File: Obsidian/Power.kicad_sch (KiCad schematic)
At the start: 79 parts, among them J10 Barrel_Jack_Switch, Q4 DMP3013SFV, U10 TPSM863257RDXR, U11 TPSM863257RDXR, U18 TLV77325PDBVR, U20 RT9045AGSP / AP2303, U23 NCV59801CML120TCG, U24 SN74LVC1G07DBV, U25 SN74LVC1G07DBV, U4 TPSM863257RDXR, U5 TPSM863257RDXR, U6 TPSM863257RDXR

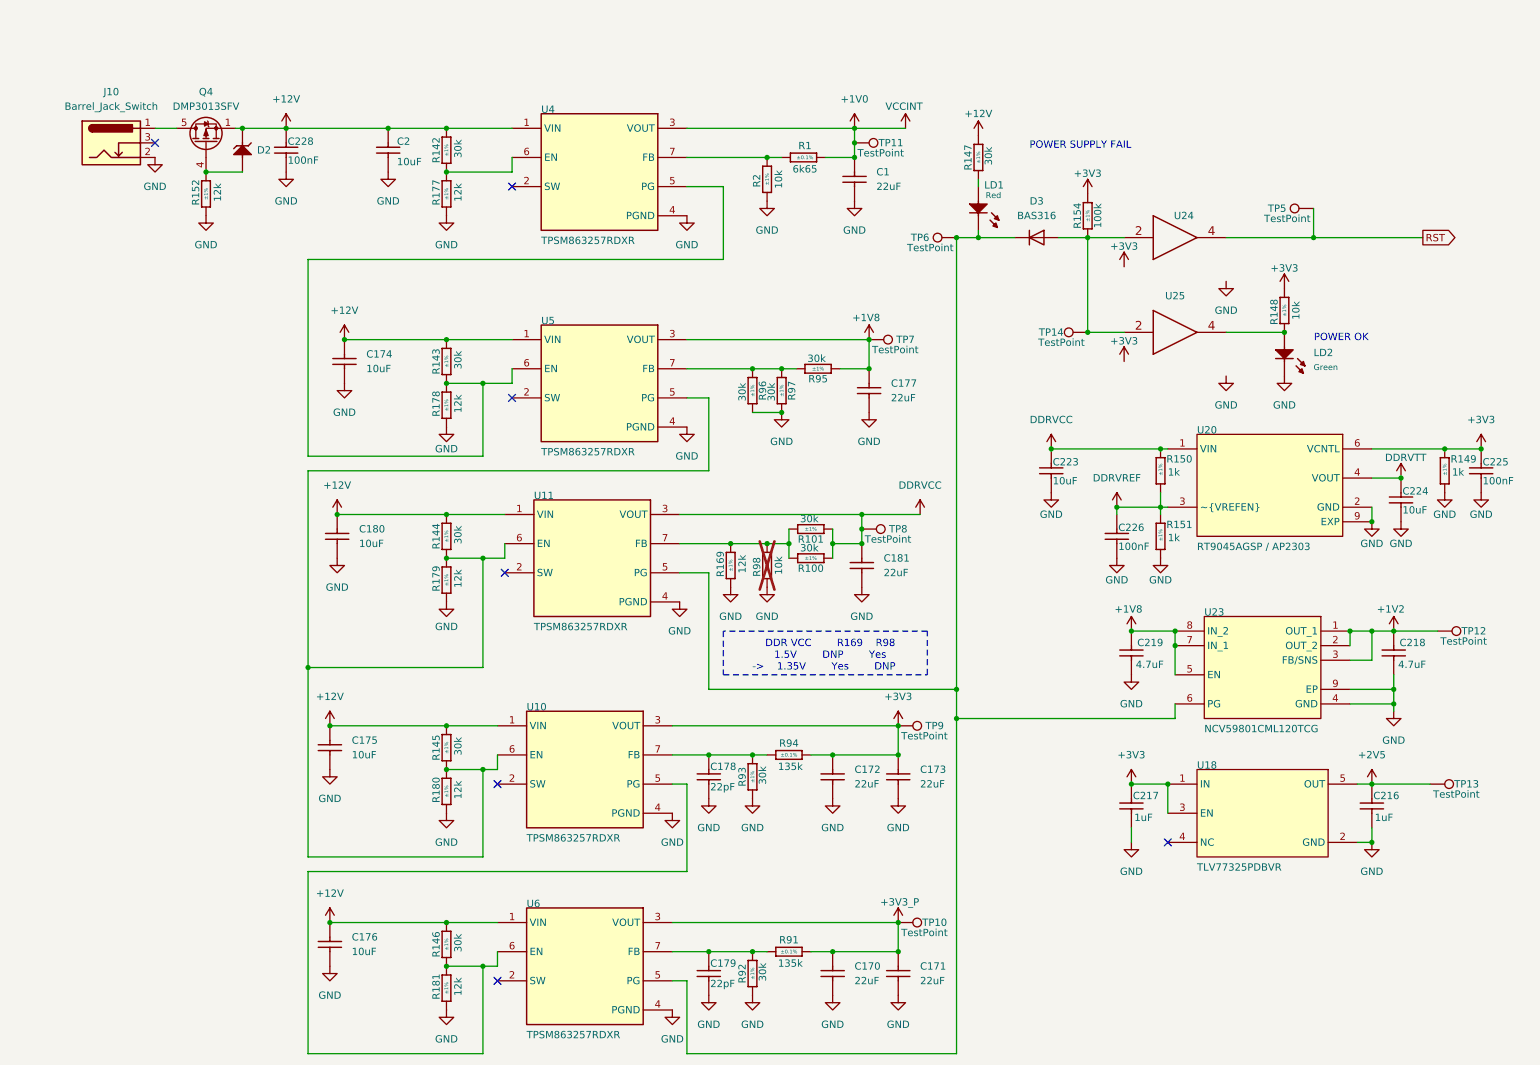
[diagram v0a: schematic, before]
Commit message: update with available components on LCSC
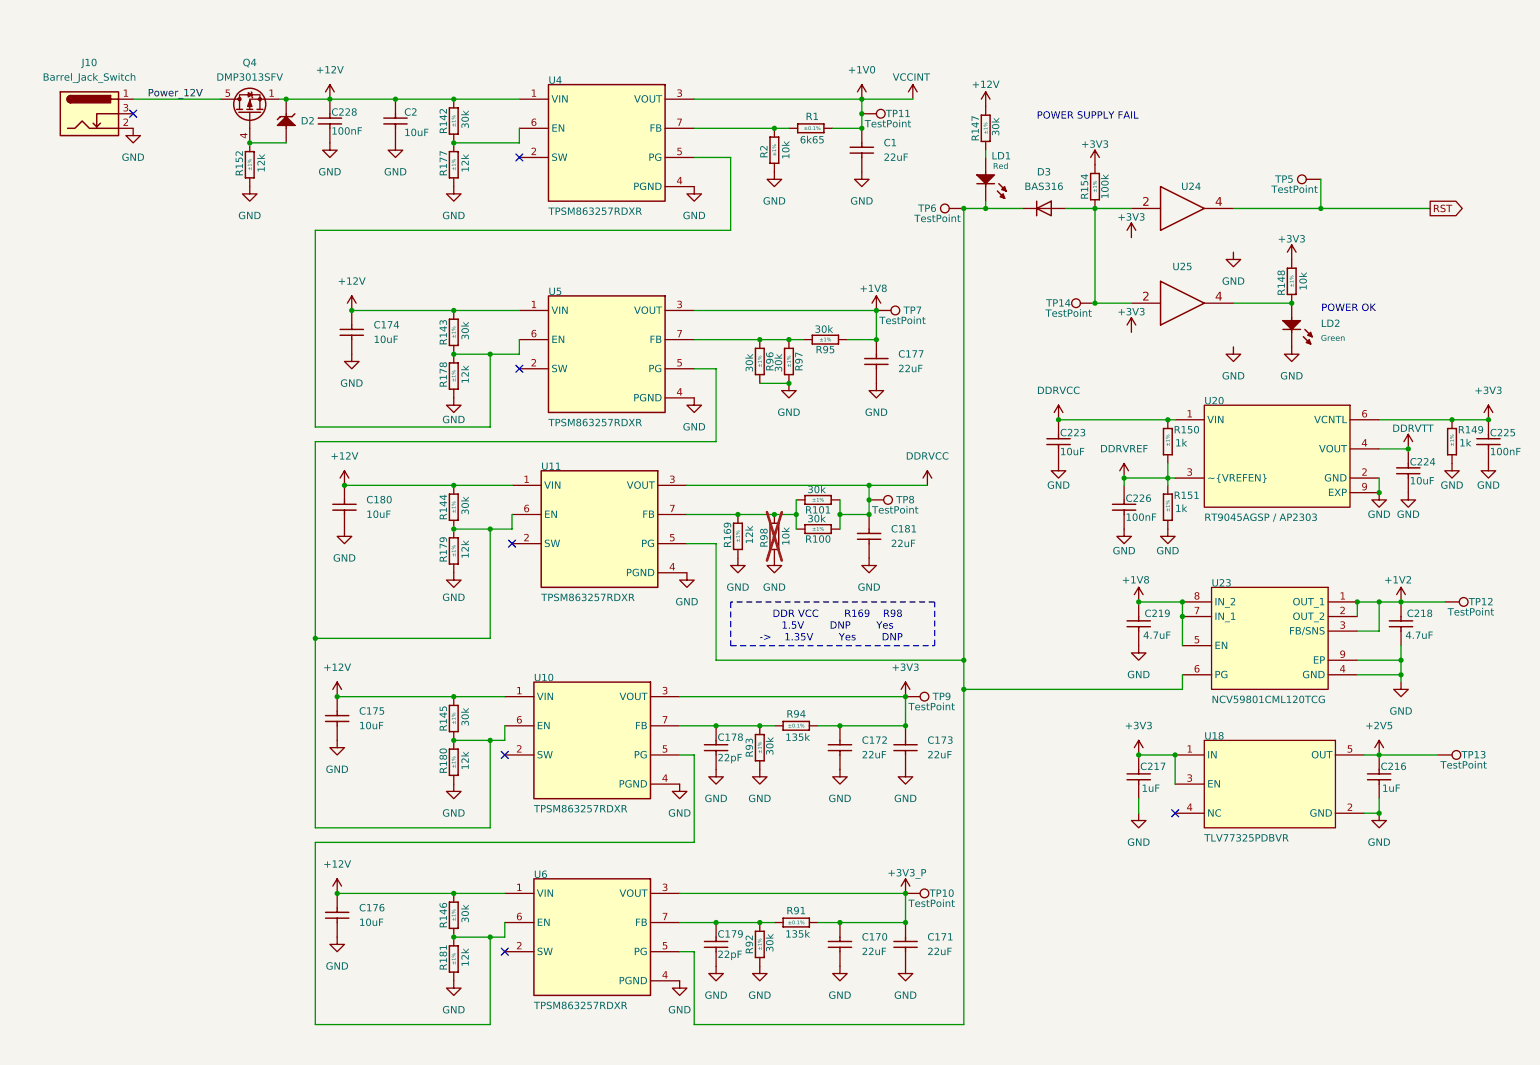
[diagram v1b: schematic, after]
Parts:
- C1, C170, C171, C172, C173, C177, C181: LCSC (none) -> C296720
- C174, C175, C176, C180, C2: LCSC (none) -> C15850
- C178, C179: LCSC (none) -> C1555
- C216, C217: LCSC (none) -> C29266
- C218, C219: LCSC (none) -> C318563
- C223, C224: LCSC (none) -> C76991
- C225, C226, C228: LCSC (none) -> C110251
- D2: FT Rotation Offset (none) -> 0; LCSC (none) -> C891576
- D3: FT Rotation Offset (none) -> 0; LCSC (none) -> C7502720
- J10: LCSC (none) -> C5155559
- LD1: FT Rotation Offset (none) -> 0; LCSC (none) -> C2899996
- LD2: LCSC (none) -> C5879295
- Q4: FT Rotation Offset (none) -> 270; LCSC (none) -> C264098
- R100, R101, R142, R143, R144, R145, R146, R147, R92, R93, R95, R96, R97: LCSC (none) -> C25776
- R148, R2, R98: LCSC (none) -> C60490
- R149, R150, R151: LCSC (none) -> C11702
- R152, R169, R177, R178, R179, R180, R181: LCSC (none) -> C2909316
- R154: LCSC (none) -> C60491
- U10, U11, U4, U5, U6: FT Rotation Offset (none) -> 0; LCSC (none) -> C19190416
- U18: FT Rotation Offset (none) -> 000; LCSC (none) -> C34443490
- U20: FT Rotation Offset (none) -> 270; LCSC (none) -> C3249960
- U24, U25: FT Rotation Offset (none) -> 180; LCSC (none) -> C7829
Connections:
- net Power_12V: now reaches J10.1, Q4.5 (D)
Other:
- moved on the sheet: C1, C170, C171, C172, C173, C174, C175, C176, C177, C178, C179, C180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

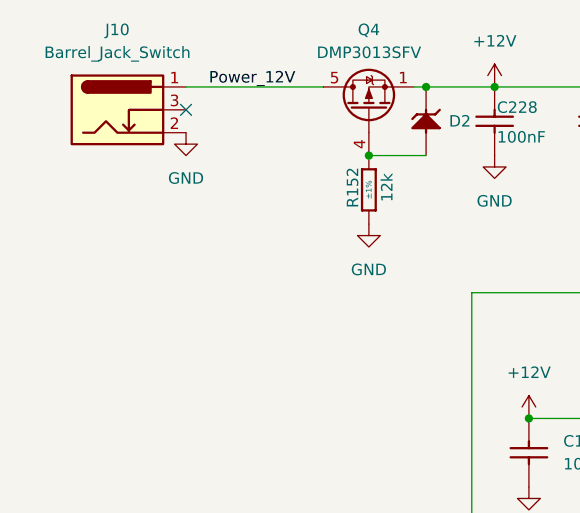
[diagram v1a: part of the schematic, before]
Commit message: adding wago
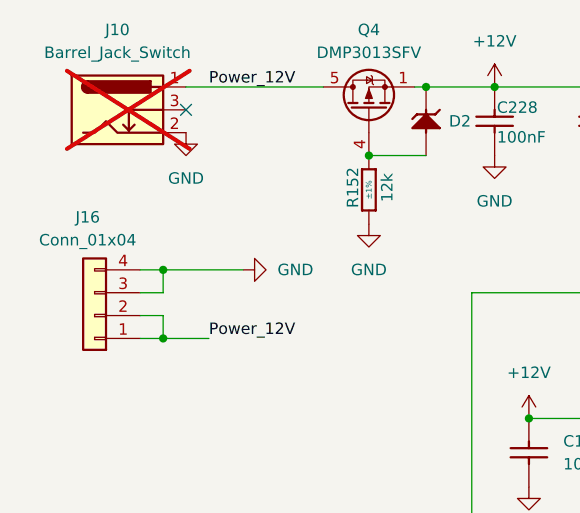
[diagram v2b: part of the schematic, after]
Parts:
- added J16: Conn_01x04, Footprint:CONN-TH_2604-1104, symbol Connector_Generic:Conn_01x04
- J10: now not fitted
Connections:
- net GND: now also J16.3 (Pin_3), J16.4 (Pin_4)
- net Power_12V: now also J16.1 (Pin_1), J16.2 (Pin_2)
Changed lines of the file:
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@@
 	)
 	(junction
+		(at 27.94 53.34)
+		(diameter 0)
+		(color 0 0 0 0)
+	)
+	(junction
 		(at 266.7 81.28)
 		(diameter 0)
@@
 	)
 	(junction
+		(at 27.94 45.72)
+		(diameter 0)
+		(color 0 0 0 0)
+	)
+	(junction
 		(at 68.58 62.23)
 		(diameter 0)
@@
 	(wire
 		(pts
+			(xy 25.4 50.8) (xy 27.94 50.8)
+		)
+		(stroke
+			(width 0)
+			(type default)
+		)
+	)
+	(wire
+		(pts
 			(xy 92.71 171.45) (xy 92.71 186.69)
 		)
@@
 	(wire
 		(pts
+			(xy 27.94 50.8) (xy 27.94 53.34)
+		)
+		(stroke
+			(width 0)
+			(type default)
+		)
+	)
+	(wire
+		(pts
 			(xy 149.86 134.62) (xy 153.67 134.62)
 		)
@@
 	(wire
 		(pts
+			(xy 25.4 53.34) (xy 27.94 53.34)
+		)
+		(stroke
+			(width 0)
+			(type default)
+		)
+	)
+	(wire
+		(pts
 			(xy 128.27 139.7) (xy 128.27 154.94)
 		)
@@
 	(wire
 		(pts
+			(xy 27.94 48.26) (xy 27.94 45.72)
+		)
+		(stroke
+			(width 0)
+			(type default)
+		)
+	)
+	(wire
+		(pts
 			(xy 66.04 163.83) (xy 86.36 163.83)
 		)
@@
 	(wire
 		(pts
+			(xy 25.4 48.26) (xy 27.94 48.26)
+		)
+		(stroke
+			(width 0)
+			(type default)
+		)
+	)
+	(wire
+		(pts
 			(xy 62.23 154.94) (xy 62.23 186.69)
 		)
@@
 	(wire
 		(pts
+			(xy 27.94 45.72) (xy 25.4 45.72)
+		)
+		(stroke
+			(width 0)
+			(type default)
+		)
+	)
+	(wire
+		(pts
 			(xy 92.71 82.55) (xy 92.71 69.85)
 		)
@@
 	(wire
 		(pts
+			(xy 36.83 45.72) (xy 27.94 45.72)
+		)
+		(stroke
+			(width 0)
+			(type default)
+		)
+	)
+	(wire
+		(pts
 			(xy 175.26 123.19) (xy 175.26 128.27)
 		)
@@
 		)
 	)
+	(wire
+		(pts
+			(xy 27.94 53.34) (xy 33.02 53.34)
+		)
+		(stroke
+			(width 0)
+			(type default)
+		)
+	)
+	(label "Power_12V"
+		(at 33.02 53.34 0)
+		(effects
+			(font
+				(size 1.27 1.27)
+			)
+			(justify left bottom)
+		)
+	)
 	(label "Power_12V"
 		(at 33.02 25.4 0)
@@
 		(exclude_from_sim no)
 		(in_bom yes)
-		(on_board yes)
-		(dnp no)
+		(on_board no)
+		(dnp yes)
 		(property "Reference" "J10"
 			(at 22.86 19.05 0)
@@
 	(symbol
 		(lib_id "power:GND")
+		(at 36.83 45.72 90)
+		(unit 1)
+		(exclude_from_sim no)
+		(in_bom yes)
+		(on_board yes)
+		(dnp no)
+		(fields_autoplaced yes)
+		(property "Reference" "#PWR0353"
+			(at 43.18 45.72 0)
+			(effects
+				(font
+					(size 1.27 1.27)
+				)
+				(hide yes)
+			)
+		)
+		(property "Value" "GND"
+			(at 40.64 45.7199 90)
+			(effects
+				(font
+					(size 1.27 1.27)
+				)
+				(justify right)
+			)
+		)
+		(property "Footprint" ""
+			(at 36.83 45.72 0)
+			(effects
+				(font
+					(size 1.27 1.27)
+				)
+				(hide yes)
+			)
+		)
+		(property "Datasheet" ""
+			(at 36.83 45.72 0)
+			(effects
+				(font
+					(size 1.27 1.27)
+				)
+				(hide yes)
+			)
+		)
+		(property "Description" "Power symbol creates a global label with name \"GND\" , ground"
+			(at 36.83 45.72 0)
+			(effects
+				(font
+					(size 1.27 1.27)
+				)
+				(hide yes)
+			)
+		)
+		(pin "1"
+		)
+		(instances
+			(project "Obsidian"
+				(path "/c2a4f786-b14c-434a-acf7-b20fb2221b0b/1f98e56a-3346-4f12-a356-5cd64c4ccde0"
+					(reference "#PWR0353")
+					(unit 1)
+				)
+			)
+		)
+	)
+	(symbol
+		(lib_id "power:GND")
 		(at 127 107.95 0)
 		(unit 1)
@@
 					(unit 1)
 				)
+			)
+		)
+	)
+	(symbol
+		(lib_id "Connector_Generic:Conn_01x04")
+		(at 20.32 50.8 180)
+		(unit 1)
+		(exclude_from_sim no)
+		(in_bom yes)
+		(on_board yes)
+		(dnp no)
+		(property "Reference" "J16"
+			(at 19.558 39.878 0)
+			(effects
+				(font
+					(size 1.27 1.27)
+				)
+			)
+		)
+		(property "Value" "Conn_01x04"
+			(at 19.558 42.418 0)
+			(effects
+				(font
+					(size 1.27 1.27)
+				)
+			)
+		)
+		(property "Footprint" "Footprint:CONN-TH_2604-1104"
+			(at 20.32 50.8 0)
+			(effects
+				(font
+					(size 1.27 1.27)
+				)
+				(hide yes)
+			)
+		)
+		(property "Datasheet" "~"
+			(at 20.32 50.8 0)
+			(effects
+				(font
+					(size 1.27 1.27)
+				)
+				(hide yes)
+			)
+		)
+		(property "Description" "Generic connector, single row, 01x04, script generated (kicad-library-utils/schlib/autogen/connector/)"
+			(at 20.32 50.8 0)
+			(effects
+				(font
+					(size 1.27 1.27)
+				)
+				(hide yes)
+			)
+		)
+		(pin "1"
+		)
+		(pin "4"
+		)
+		(pin "2"
+		)
+		(pin "3"
+		)
+		(instances
+			(project ""
+				(path "/c2a4f786-b14c-434a-acf7-b20fb2221b0b/1f98e56a-3346-4f12-a356-5cd64c4ccde0"
+					(reference "J16")
+					(unit 1)
+				)
